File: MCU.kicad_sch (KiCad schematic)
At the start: 20 parts, among them J801 Conn_01x03_Pin, J802 Conn_02x02_Odd_Even, Q801 BSS138, Q802 BSS138, U801 ISO6721RFBD, U802 ATtiny1614-SS

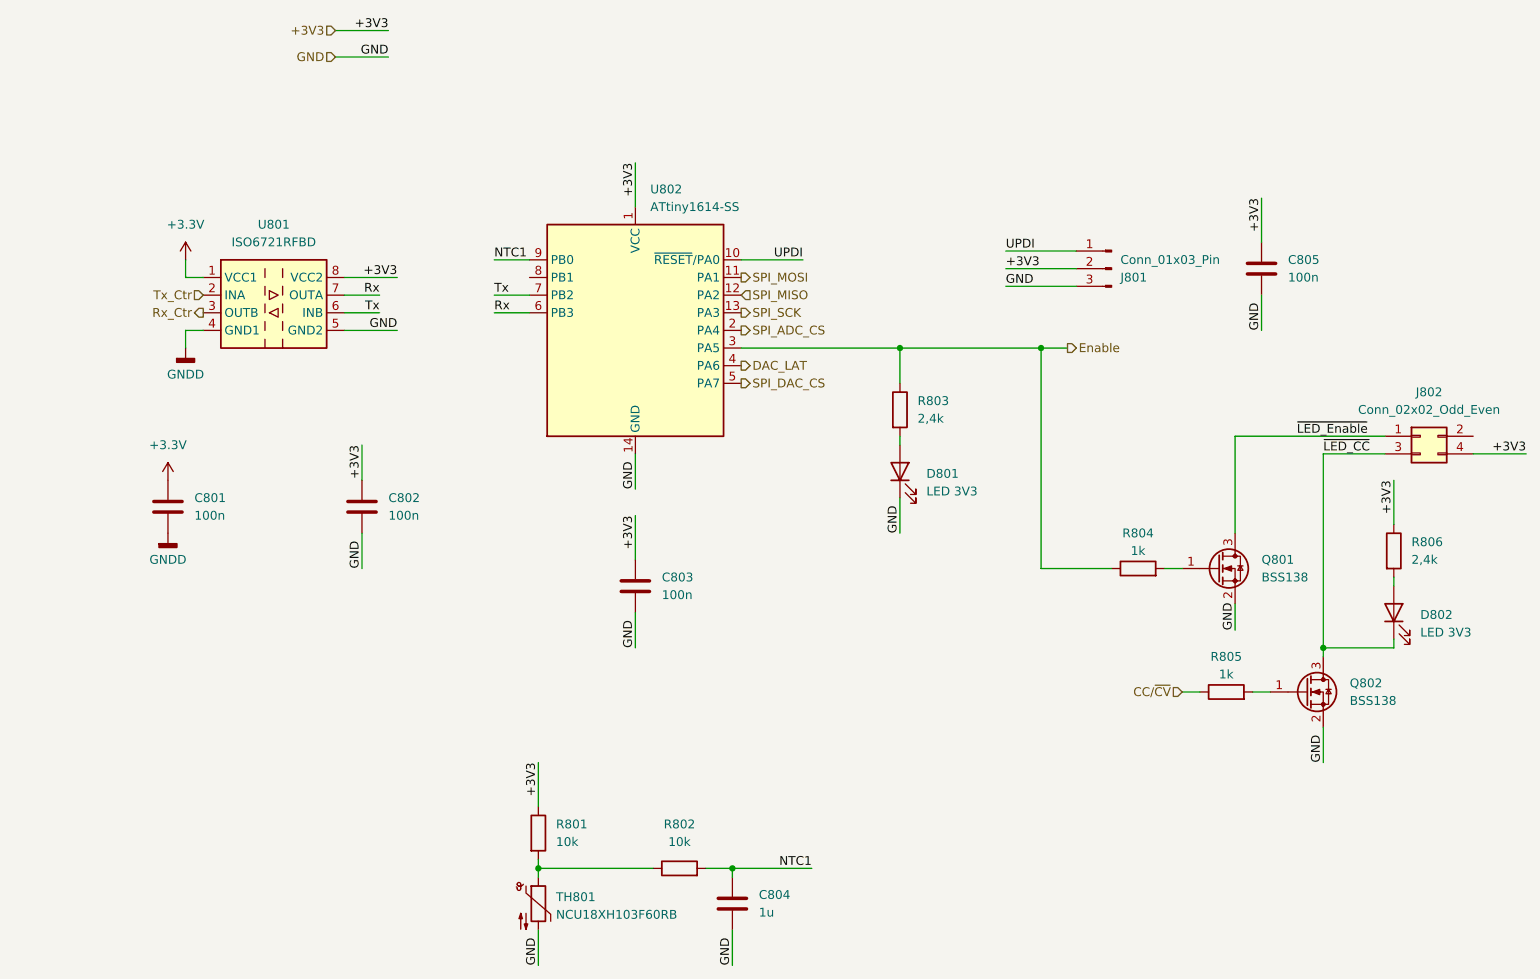
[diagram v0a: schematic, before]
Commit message: added loop calc
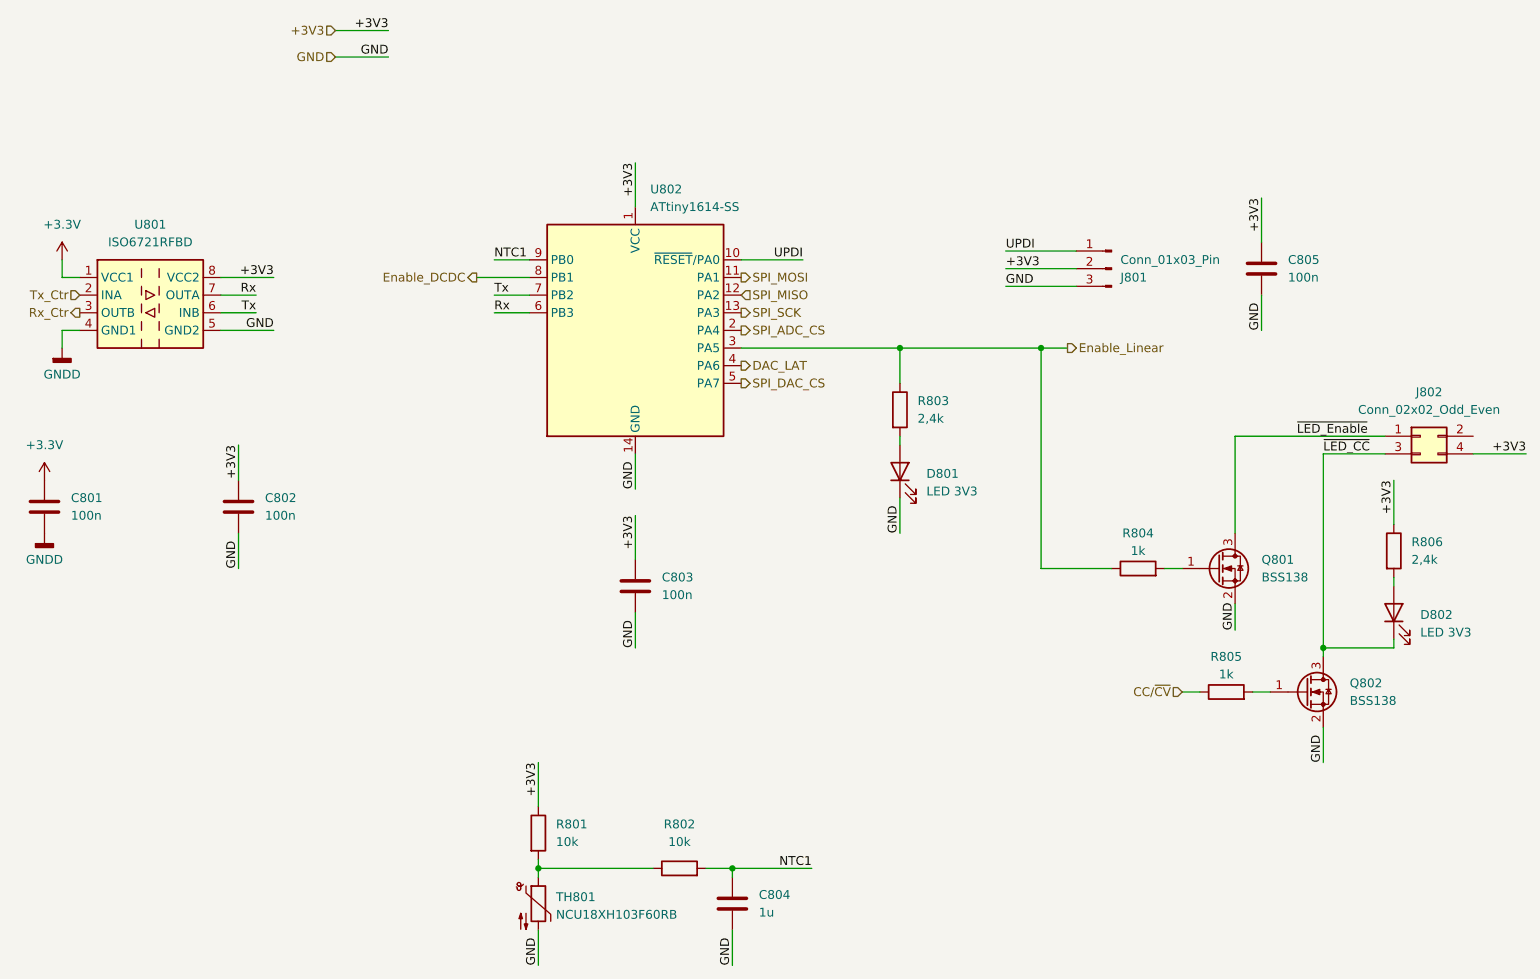
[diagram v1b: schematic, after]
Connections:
- net Enable_DCDC: now reaches U802.8 (PB1)
- net Enable renamed Enable_Linear
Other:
- moved on the sheet: C801, C802, U801
